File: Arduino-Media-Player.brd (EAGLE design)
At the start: 100 x 50 mm, 41 parts, among them U1 ATMEGA328P, U2 FT232RLSSOP, U3 DS1307SO8, U4 AMS117-33, U5 AMS117-18, U6 VS1053B, U7 74HC4050 LVL CONVERTER

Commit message: update
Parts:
- removed U$1: MICRO-SD-CARD-EBAY, SparkFun-Connectors:MICRO-SD-EBAY
- added J1: MICRO-SD-CARD, SparkFun-Connectors-EDITED:MICRO-SD-EBAY
- added R102, R105, R110, R111: 100K, SparkFun-Passives:0805
- moved U7 8.03 mm to (47.3, 44.8)
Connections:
- net 3.3V: now also J1.4, R102.2, R105.2
- net GND: now also J1.10, J1.11, J1.12, J1.6, J1.9, R110.1, R111.1
- net GPIO0: now also R111.2
- net GPIO1: now also R110.2
- net MIDI-RX: now also R102.1
- net MISO: now also J1.7
- net MOSI: now also J1.3
- net MP3-RST: now also R105.1
- net SCK: now also J1.5
- net SD-CS: now also J1.2

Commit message: update
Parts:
- removed R10: 10K, rcl:R0805W
- added R5: 10K, SparkFun-Passives:0805
- R1, R2: device rcl:R0805W -> SparkFun-Passives:0805
- moved R2 123.1 mm to (-45.7, -34.3), turned to 0 degrees
- moved R1 117.8 mm to (-41.9, -34.3), turned to 0 degrees
- moved C11 97.7 mm to (80.0, 5.08), turned to 180 degrees
- moved C12 89.2 mm to (65.4, 16.5)
- moved C10 76.8 mm to (40.6, 44.5), turned to 90 degrees
- moved R101 58.7 mm to (44.5, 30.5), turned to 270 degrees
- moved C108 58.1 mm to (35.6, 33.0), turned to 90 degrees
- moved C103 52.5 mm to (35.6, 27.9), turned to 270 degrees
- moved XTAL3 48.5 mm to (40.6, 30.5), turned to 270 degrees
- moved R112 29.7 mm to (54.6, 21.6), turned to 0 degrees
- moved R104 24.1 mm to (49.5, 21.6), turned to 180 degrees
- moved R103 13.3 mm to (47.0, 38.1)
- moved U6 12.3 mm to (51.8, 30.9), turned to 180 degrees
- moved U1 8.52 mm to (52.1, 14.0)
- moved C1 7.84 mm to (31.8, 17.8)
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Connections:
- net /RESET: now also R5.1; no longer R10.1
- net 5V: now also R5.2; no longer R10.2
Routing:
- net 3.3V: track 0.00 -> 0.71 mm

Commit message: Added audio output circuitry for mp3 decoder
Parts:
- added C101, C102: 220uF, SparkFun-Passives:PANASONIC_G
- added C110: .1uF, SparkFun-Passives:0805
- added C8: 47nF, SparkFun-Passives:0805
- added C9: 10nF, SparkFun-Passives:0805
- added R106, R107: 20, SparkFun-Passives:0805
- added R109: 10, SparkFun-Passives:0805
- added R120, R121: 100, SparkFun-Passives:0805
- added R13, R14: 1K, SparkFun-Passives:0805
- added SJ1, SJ2: (no value), SparkFun-Passives:PAD-JUMPER-2-NO_YES_SILK_ROUND
- C10: value .1uF -> 10nF
- moved C10 155.2 mm to (-83.8, -48.3), turned to 0 degrees
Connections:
- new net 5V-GPIO1: SJ2.1, U1.2
- new net 5V-MIDI-RX: SJ1.1, U1.1
- new net A0: U1.23
- new net A1: U1.24
- new net A2: U1.25
- new net A3: U1.26
- new net A6: U1.19
- new net A7: U1.22
- new net LEFT-OUT: C101.-
- new net N$1: R13.1, SJ1.2
- new net N$14: C102.+, R121.1
- new net N$15: C8.2, R109.1
- new net N$17: C9.2, R106.1
- new net N$18: C10.2, R107.1
- new net N$2: R14.1, SJ2.2
- new net N$3: C101.+, R120.2
- new net RIGHT-OUT: C102.-
- net 3.3V: now also C110.1; no longer C10.1
- net 5V-MOSI: now also U1.15
- net 5V-MP3-CS: now also U1.10
- net 5V-MP3-DCS: now also U1.11
- net 5V-MP3-RST: now also U1.12
- net 5V-SCK: now also U1.17
- net 5V-SD-CS: now also U1.13
- net GBUF: now also R109.2
- net GND: now also C10.1, C110.2, C8.1, C9.1; no longer C10.2
- net GPIO1: now also R14.2
- net LEFT: now also R107.2, R120.1
- net MIDI-RX: now also R13.2
- net MP3-DREQ: now also U1.32
- net RIGHT: now also R106.2, R121.2

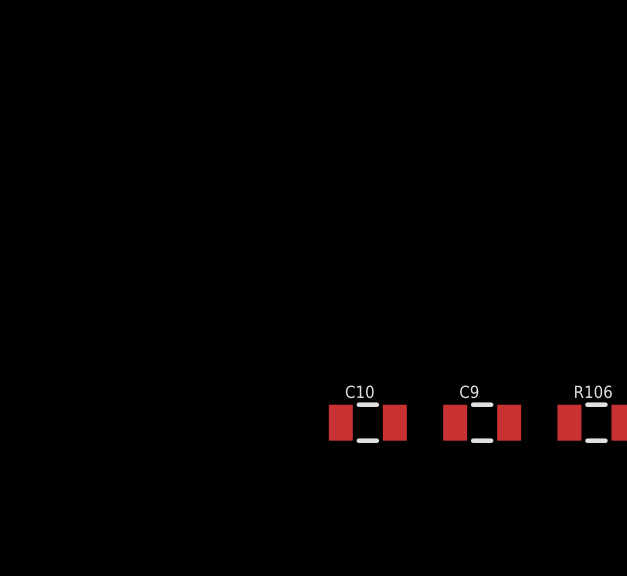
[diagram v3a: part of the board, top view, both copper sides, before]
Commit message: Added ICSP header for ATMEGA328p
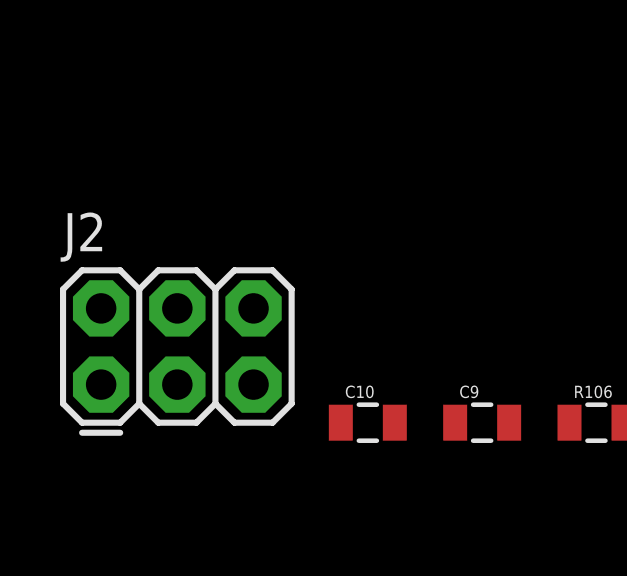
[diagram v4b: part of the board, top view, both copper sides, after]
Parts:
- added J2: ICSP, SparkFun-Connectors-EDITED:2X3
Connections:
- net /RESET: now also J2.5
- net 5V: now also J2.2
- net 5V-MOSI: now also J2.4
- net 5V-SCK: now also J2.3
- net GND: now also J2.6
- net MISO: now also J2.1
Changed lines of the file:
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@@
 <attribute name="CREVISION" value="A" x="-83.82" y="-48.26" size="1.778" layer="27" display="off"/>
 </element>
+<element name="J2" library="SparkFun-Connectors-EDITED" package="2X3" value="ICSP" x="-92.71" y="-46.99"/>
 </elements>
 <signals>
@@
 <contactref element="C9" pad="1"/>
 <contactref element="C10" pad="1"/>
+<contactref element="J2" pad="6"/>
 <wire x1="-80.91" y1="-48.26" x2="-84.72" y2="-48.26" width="0" layer="19" extent="1-1"/>
+<wire x1="-87.63" y1="-44.45" x2="-84.72" y2="-48.26" width="0" layer="19" extent="1-1"/>
 <wire x1="-69.48" y1="-48.26" x2="-80.91" y2="-48.26" width="0" layer="19" extent="1-1"/>
 <wire x1="-35.19" y1="-34.29" x2="-69.48" y2="-48.26" width="0" layer="19" extent="1-1"/>
@@
 <contactref element="R2" pad="2"/>
 <contactref element="PTC1" pad="2"/>
-<wire x1="80.91" y1="5.08" x2="82.6262" y2="12.065" width="0" layer="19" extent="1-1"/>
-<wire x1="56.3626" y1="11.97" x2="80.91" y2="5.08" width="0" layer="19" extent="1-1"/>
-<wire x1="56.3626" y1="13.57" x2="56.3626" y2="11.97" width="0" layer="19" extent="1-1"/>
-<wire x1="47.7774" y1="12.77" x2="56.3626" y2="11.97" width="0" layer="19" extent="1-1"/>
-<wire x1="47.7774" y1="14.37" x2="47.7774" y2="12.77" width="0" layer="19" extent="1-1"/>
-<wire x1="31.75" y1="24.3475" x2="47.7774" y2="14.37" width="0" layer="19" extent="1-1"/>
-<wire x1="26.67" y1="30.11" x2="31.75" y2="24.3475" width="0" layer="19" extent="1-1"/>
-<wire x1="26.3" y1="34.29" x2="26.67" y2="30.11" width="0" layer="19" extent="1-1"/>
-<wire x1="26.3" y1="39.37" x2="26.3" y2="34.29" width="0" layer="19" extent="1-1"/>
-<wire x1="18.896" y1="37.125" x2="26.3" y2="39.37" width="0" layer="19" extent="1-1"/>
+<contactref element="J2" pad="2"/>
+<wire x1="-44.82" y1="-34.29" x2="-92.71" y2="-44.45" width="0" layer="19" extent="1-1"/>
+<wire x1="-41.01" y1="-34.29" x2="-44.82" y2="-34.29" width="0" layer="19" extent="1-1"/>
+<wire x1="-37.2" y1="-34.29" x2="-41.01" y2="-34.29" width="0" layer="19" extent="1-1"/>
+<wire x1="11.9888" y1="25.1714" x2="-37.2" y2="-34.29" width="0" layer="19" extent="1-1"/>
+<wire x1="18.896" y1="37.125" x2="11.9888" y2="25.1714" width="0" layer="19" extent="1-1"/>
+<wire x1="26.3" y1="39.37" x2="18.896" y2="37.125" width="0" layer="19" extent="1-1"/>
+<wire x1="26.3" y1="34.29" x2="26.3" y2="39.37" width="0" layer="19" extent="1-1"/>
+<wire x1="26.67" y1="30.11" x2="26.3" y2="34.29" width="0" layer="19" extent="1-1"/>
+<wire x1="31.75" y1="24.3475" x2="26.67" y2="30.11" width="0" layer="19" extent="1-1"/>
 <wire x1="11.584" y1="40.375" x2="18.896" y2="37.125" width="0" layer="19" extent="1-1"/>
 <wire x1="8.52" y1="44.45" x2="11.584" y2="40.375" width="0" layer="19" extent="1-1"/>
-<wire x1="11.9888" y1="25.1714" x2="18.896" y2="37.125" width="0" layer="19" extent="1-1"/>
-<wire x1="-37.2" y1="-34.29" x2="11.9888" y2="25.1714" width="0" layer="19" extent="1-1"/>
-<wire x1="-41.01" y1="-34.29" x2="-37.2" y2="-34.29" width="0" layer="19" extent="1-1"/>
-<wire x1="-44.82" y1="-34.29" x2="-41.01" y2="-34.29" width="0" layer="19" extent="1-1"/>
+<wire x1="47.7774" y1="14.37" x2="31.75" y2="24.3475" width="0" layer="19" extent="1-1"/>
+<wire x1="47.7774" y1="12.77" x2="47.7774" y2="14.37" width="0" layer="19" extent="1-1"/>
+<wire x1="56.3626" y1="13.57" x2="47.7774" y2="14.37" width="0" layer="19" extent="1-1"/>
+<wire x1="56.3626" y1="11.97" x2="56.3626" y2="13.57" width="0" layer="19" extent="1-1"/>
+<wire x1="80.91" y1="5.08" x2="56.3626" y2="11.97" width="0" layer="19" extent="1-1"/>
+<wire x1="82.6262" y1="12.065" x2="80.91" y2="5.08" width="0" layer="19" extent="1-1"/>
 </signal>
 <signal name="SQW">
@@
 <contactref element="U7" pad="3"/>
 <contactref element="U1" pad="15"/>
-<wire x1="54.07" y1="9.6774" x2="45.4025" y2="41.9675" width="0" layer="19" extent="1-1"/>
+<contactref element="J2" pad="4"/>
+<wire x1="54.07" y1="9.6774" x2="-90.17" y2="-44.45" width="0" layer="19" extent="1-1"/>
+<wire x1="45.4025" y1="41.9675" x2="54.07" y2="9.6774" width="0" layer="19" extent="1-1"/>
 </signal>
 <signal name="5V-SD-CS">
@@
 <contactref element="U7" pad="7"/>
 <contactref element="U1" pad="17"/>
-<wire x1="56.3626" y1="11.17" x2="50.4825" y2="41.9675" width="0" layer="19" extent="1-1"/>
+<contactref element="J2" pad="3"/>
+<wire x1="56.3626" y1="11.17" x2="-90.17" y2="-46.99" width="0" layer="19" extent="1-1"/>
+<wire x1="50.4825" y1="41.9675" x2="56.3626" y2="11.17" width="0" layer="19" extent="1-1"/>
 </signal>
 <signal name="5V-MP3-CS">
@@
 <contactref element="U1" pad="29"/>
 <contactref element="R5" pad="1"/>
-<wire x1="51.67" y1="18.2626" x2="66.305" y2="16.51" width="0" layer="19" extent="1-1"/>
-<wire x1="-39" y1="-34.29" x2="51.67" y2="18.2626" width="0" layer="19" extent="1-1"/>
+<contactref element="J2" pad="5"/>
+<wire x1="-39" y1="-34.29" x2="-87.63" y2="-46.99" width="0" layer="19" extent="1-1"/>
+<wire x1="51.67" y1="18.2626" x2="-39" y2="-34.29" width="0" layer="19" extent="1-1"/>
+<wire x1="66.305" y1="16.51" x2="51.67" y2="18.2626" width="0" layer="19" extent="1-1"/>
 </signal>
 <signal name="RCAP">
@@
 <contactref element="U1" pad="16"/>
 <contactref element="J1" pad="7"/>
-<wire x1="51.51" y1="26.62" x2="61.95" y2="40.64" width="0" layer="19" extent="1-1"/>
-<wire x1="54.87" y1="9.6774" x2="51.51" y2="26.62" width="0" layer="19" extent="1-1"/>
+<contactref element="J2" pad="1"/>
+<wire x1="54.87" y1="9.6774" x2="-92.71" y2="-46.99" width="0" layer="19" extent="1-1"/>
+<wire x1="51.51" y1="26.62" x2="54.87" y2="9.6774" width="0" layer="19" extent="1-1"/>
+<wire x1="61.95" y1="40.64" x2="51.51" y2="26.62" width="0" layer="19" extent="1-1"/>
 </signal>
 <signal name="MP3-DREQ">
